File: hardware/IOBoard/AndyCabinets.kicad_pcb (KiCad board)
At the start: 2 copper layers, 44.5 x 76.2 mm, 47 parts, among them SW1 Mode_Encoder, SW2 Color_Encoder, U1 74HC14

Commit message: After PCB v2
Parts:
- removed C9: 1uF, Capacitor_SMD:C_0805_2012Metric
- C11, C13: value 0.01uF -> 0.1uF
- moved C6 47.8 mm to (176.1, 115.9)
- moved R2 47.8 mm to (176.1, 120.0)
- moved R6 47.8 mm to (176.1, 117.9)
- moved C5 47.7 mm to (177.8, 115.9)
- moved R1 47.7 mm to (177.8, 120.0)
- moved R5 47.7 mm to (177.8, 117.9)
- moved C11 47.3 mm to (179.5, 115.9)
- moved R10 47.3 mm to (179.5, 117.9)
- moved R9 47.3 mm to (179.5, 120.0)
- moved C7 30.3 mm to (216.1, 64.9), turned to 0 degrees
- moved C8 29.0 mm to (216.1, 66.4), turned to 0 degrees
- moved R7 28.6 mm to (214.1, 64.9), turned to 0 degrees
- moved C13 27.7 mm to (216.1, 67.8), turned to 0 degrees
- moved R8 27.2 mm to (214.1, 66.4), turned to 180 degrees
- moved R3 27.2 mm to (212.0, 64.9), turned to 0 degrees
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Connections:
- U1 pad 12: Net-(C13-Pad1) -> /GPIO32_MODE_BTN
- U1 pad 13: /GPIO32_MODE_BTN -> Net-(C13-Pad1)
- U1 pad 3: /GPIO33_MODE_B -> Net-(C7-Pad1)
- U1 pad 4: Net-(C7-Pad1) -> /GPIO33_MODE_B
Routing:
- net +3V3: track 122.2 -> 48.3 mm, vias 13 -> 1
- net Net-(C5-Pad1): track 38.5 -> 84.1 mm, vias 0 -> 2
- net Net-(C11-Pad1): track 32.2 -> 77.5 mm, vias 0 -> 2
- net Net-(C6-Pad1): track 36.3 -> 81.0 mm, vias 0 -> 4
- net Net-(R10-Pad2): track 60.7 -> 17.5 mm, vias 0 -> 1
- net Net-(R1-Pad2): track 54.0 -> 18.8 mm, vias 0 -> 2
- net Net-(R2-Pad2): track 48.8 -> 17.5 mm, vias 0 -> 2
- net Net-(C8-Pad1): track 40.5 -> 14.6 mm, vias 0 -> 2
- net GNDD: track 74.3 -> 99.1 mm, vias 21 -> 20
- net Net-(C13-Pad1): track 34.2 -> 9.48 mm, vias 0 -> 2
- net +5V: track 46.3 -> 22.6 mm
- net /GPIO35_COLOR_BTN: track 50.9 -> 27.8 mm
- net /GPIO32_MODE_BTN: track 33.1 -> 12.3 mm
- net /GPIO39_COLOR_A: track 44.9 -> 26.5 mm
- net Net-(R3-Pad2): track 24.3 -> 42.1 mm, vias 0 -> 3
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- added copper zone on F.Cu, net +3V3
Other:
- board size 44.5 x 76.2 mm -> 44.4 x 70 mm
- net class Default: clearance 0.1016 -> 0.1524; trace_width 0.127 -> 0.2032
- net class Power: clearance 0.2 -> 0.1524; trace_width 0.5 -> 0.3556
- rule trace_clearance: 0.1016 -> 0.1524

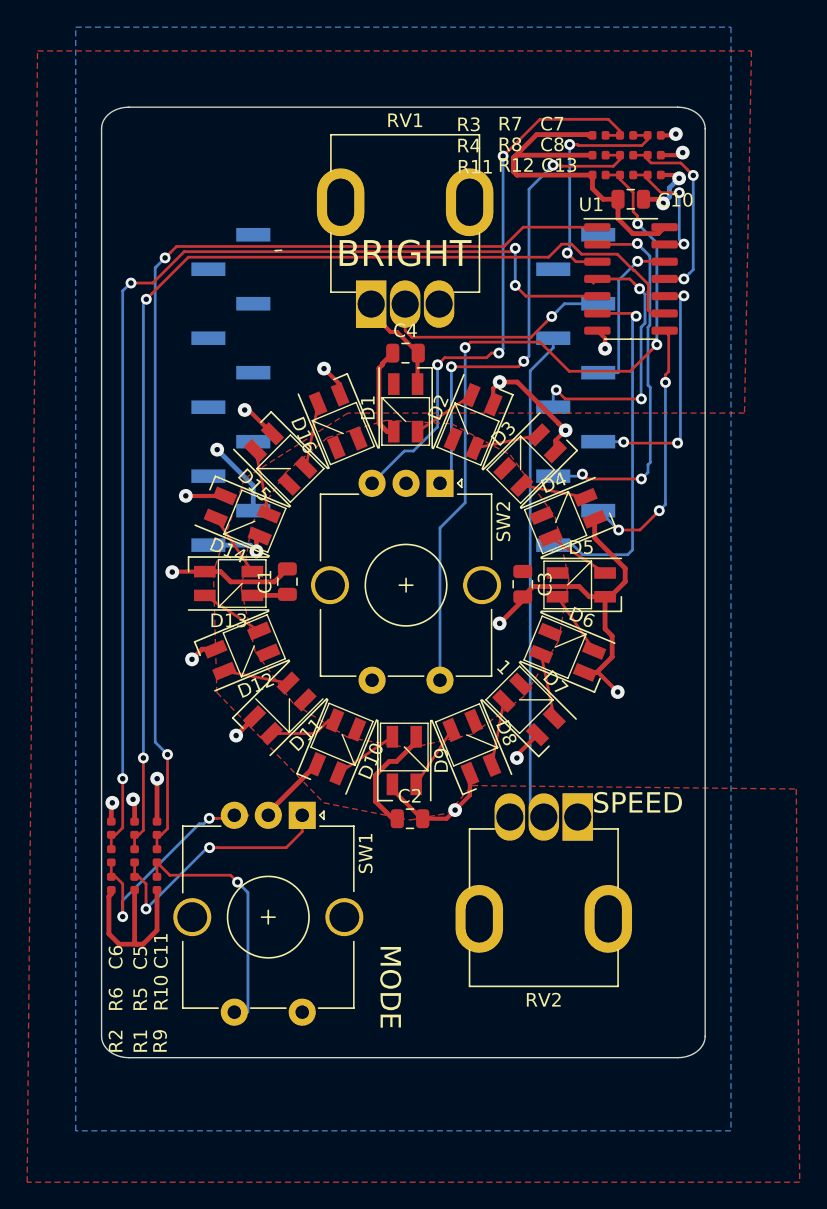
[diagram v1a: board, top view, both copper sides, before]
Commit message: Initial working remote version; some minor PCB changes
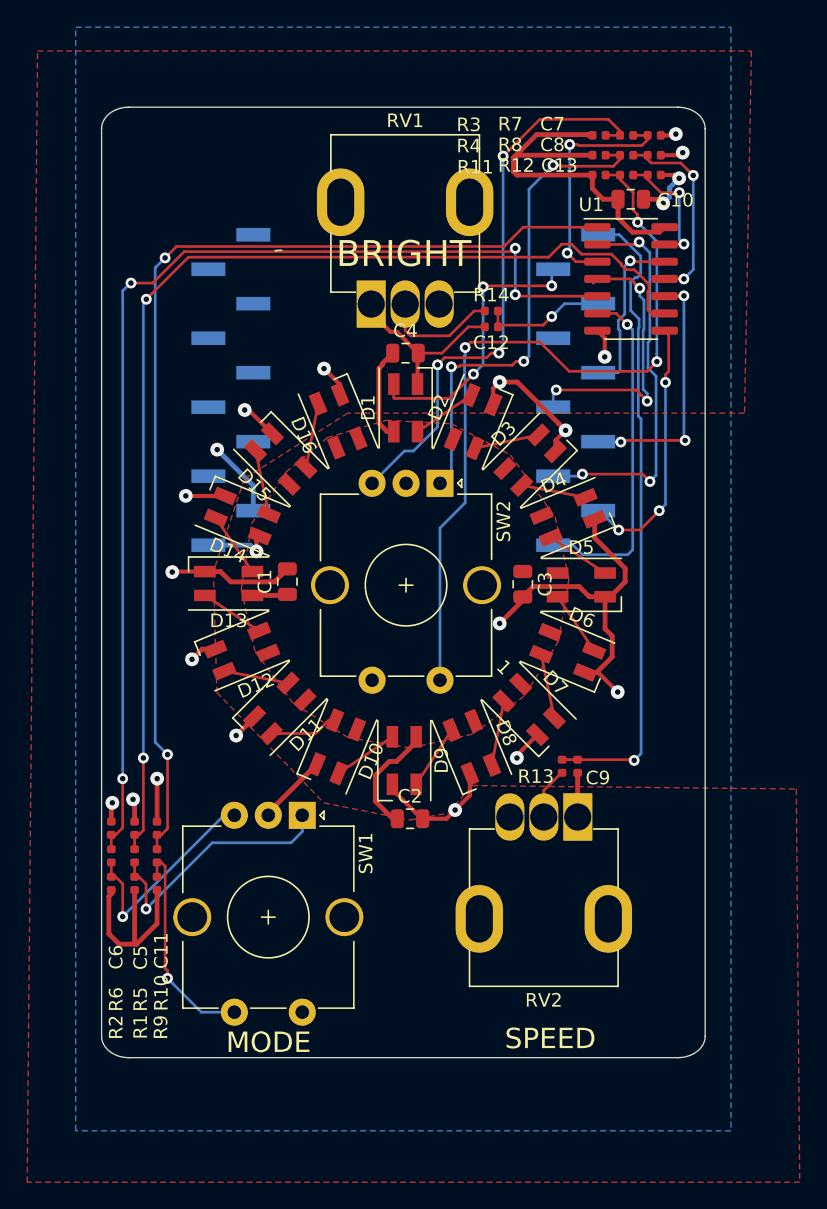
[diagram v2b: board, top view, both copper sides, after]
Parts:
- added C12: 0.1uF, Capacitor_SMD:C_0402_1005Metric, F.Cu at (204.1, 79.0)
- added C9: 0.1uF, Capacitor_SMD:C_0402_1005Metric, F.Cu at (210.5, 111.4)
- added R13: 10K, Resistor_SMD:R_0402_1005Metric, F.Cu at (209.3, 111.4)
- added R14: 10K, Resistor_SMD:R_0402_1005Metric, F.Cu at (204.1, 77.8)
- C5, C6: value 0.01uF -> 0.1uF
- RV1: value Speed_Pot -> BrightPot
- RV2: value Bright_Pot -> SpeedPot
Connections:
- net /GPIO32_MODE_BTN renamed /GPIO32_COLOR_BTN
- net /GPIO33_MODE_B renamed /GPIO33_COLOR_B
- net /GPIO34_MODE_A renamed /GPIO34_COLOR_A
- net /GPIO35_COLOR_BTN renamed /GPIO35_MODE_BTN
- net /GPIO36_COLOR_B renamed /GPIO36_MODE_A
- net /GPIO39_COLOR_A renamed /GPIO39_MODE_B
- D1 pad 4: /GPIO32_PREVIEW -> /GPIO14_PREVIEW
- EXT2 pad 10: /GPIO13/I2C-SDA -> /GPIO13_SPEED
- EXT2 pad 7: /GPIO16_BRIGHT -> /GPIO16
- EXT2 pad 8: /GPIO15_SPEED -> /GPIO15_BRIGHT
- EXT2 pad 9: /GPIO14/HS2_CLK -> /GPIO14_PREVIEW
- RV1 pad 2: /GPIO15_SPEED -> Net-(R14-Pad1)
- RV2 pad 2: /GPIO16_BRIGHT -> Net-(R13-Pad1)
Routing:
- net /GPIO13_SPEED: track 0.00 -> 47.2 mm, vias 0 -> 1
- net /GPIO16_BRIGHT: track 36.0 -> 0.00 mm
- net /GPIO14_PREVIEW: track 0.00 -> 20.7 mm, vias 0 -> 3
- net /GPIO15_SPEED: track 17.4 -> 0.00 mm, vias 1 -> 0
- net /GPIO15_BRIGHT: track 0.00 -> 9.60 mm, vias 0 -> 1
- net GNDD: track 99.1 -> 108.6 mm
- net Net-(R14-Pad1): track 0.00 -> 8.73 mm
- net Net-(R13-Pad1): track 0.00 -> 3.84 mm
- net Net-(R2-Pad2): track 17.5 -> 15.8 mm, vias 2 -> 1
- net Net-(R10-Pad2): track 17.5 -> 16.1 mm
- net /GPIO35_MODE_BTN: track 27.8 -> 29.0 mm
- net /GPIO39_MODE_B: track 26.5 -> 25.6 mm
- net Net-(R11-Pad2): track 55.9 -> 56.7 mm
- net /GPIO33_COLOR_B: track 21.1 -> 21.9 mm
- net Net-(R1-Pad2): track 18.8 -> 19.0 mm, vias 2 -> 1
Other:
- board text added: "13 BRIGHT"
- board text added: "14 PREVIEW"
- board text removed: "HS2_CLK"
- board text removed: "I2C-SDA"

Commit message: Rev 3 PCB
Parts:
- added J1: wESP Connector, YonaFootprints:PinSocket_2x10_P2.54mm_Vertical_SMD_Mirror, B.Cu at (197.6, 129.7)
- added JP1: wESP Power Jumper, Jumper:SolderJumper-2_P1.3mm_Open_TrianglePad1.0x1.5mm, B.Cu at (198.1, 122.4)
- SW1: value Mode_Encoder -> Color_Encoder; footprint Rotary_Encoder:RotaryEncoder_Alps_EC12E-Switch_Vertical_H20mm_CircularMountingHoles -> YonaFootprints:RotaryEncoder_Alps_EC12E-SMDSwitch_Vertical_H20mm_CircularMountingHoles
- SW2: value Color_Encoder -> Mode_Encoder
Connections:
- net /GPIO14_PREVIEW renamed /GPIO14
- net /GPIO32_COLOR_BTN renamed /GPIO32
- net /GPIO35_MODE_BTN renamed /COLOR_BTN
- net /GPIO36_MODE_A renamed /COLOR_A
- net /GPIO39_MODE_B renamed /COLOR_B
- C12 pad 1: /GPIO15_BRIGHT -> /BRIGHT
- C9 pad 1: /GPIO13_SPEED -> /GPIO33
- EXT2 pad 10: /GPIO13_SPEED -> /GPIO13
- EXT2 pad 4: /GPIO34_COLOR_A -> /BRIGHT
- EXT2 pad 5: /GPIO33_COLOR_B -> /GPIO33
- EXT2 pad 8: /GPIO15_BRIGHT -> /GPIO15
- R13 pad 2: /GPIO13_SPEED -> /GPIO33
- R14 pad 2: /GPIO15_BRIGHT -> /BRIGHT
- U1 pad 10: /GPIO34_COLOR_A -> /GPIO15
- U1 pad 4: /GPIO33_COLOR_B -> /GPIO13
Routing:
- net /GPIO13: track 0.00 -> 95.3 mm, vias 0 -> 5
- net /GPIO15: track 0.00 -> 94.3 mm, vias 0 -> 4
- net /GPIO14: track 20.7 -> 102.9 mm, vias 3 -> 6
- net /GPIO33: track 0.00 -> 74.3 mm, vias 0 -> 5
- net /BRIGHT: track 0.00 -> 66.9 mm, vias 0 -> 5
- net /GPIO32: track 12.7 -> 77.3 mm, vias 1 -> 5
- net /COLOR_BTN: track 29.0 -> 85.7 mm, vias 3 -> 5
- net /COLOR_B: track 25.6 -> 75.5 mm, vias 1 -> 5
- net /GPIO13_SPEED: track 47.2 -> 0.00 mm, vias 1 -> 0
- net /COLOR_A: track 19.3 -> 61.1 mm, vias 3 -> 5
- net /GPIO33_COLOR_B: track 21.9 -> 0.00 mm, vias 3 -> 0
- net /GPIO34_COLOR_A: track 18.6 -> 0.00 mm, vias 3 -> 0
- net +5V: track 22.6 -> 39.5 mm, vias 1 -> 2
- net /wESP_V+: track 0.00 -> 13.9 mm
- net /GPIO15_BRIGHT: track 9.60 -> 0.00 mm, vias 1 -> 0
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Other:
- board size 44.4 x 70 mm -> 44.4 x 71.4 mm
- board text added: "13 MODE_B"
- board text added: "15 MODE_A"
- board text added: "16 N/C"
- board text added: "32 MODE_BTN"
- board text added: "33 SPEED"
- board text added: "34 BRIGHT"
- board text added: "35 COLOR_BTN"
- board text added: "36 COLOR_A"
- board text added: "39 COLOR_B"
- board text added: "COLOR"
- board text added: "V+"
- board text added: "wESP"
- board text removed: "13 BRIGHT"
- board text removed: "15 SPEED"
- board text removed: "16 BRIGHT"
- board text removed: "30 COLOR B"
- board text removed: "32"
- board text removed: "33 MODE B"
- board text removed: "34 MODE A"
- board text removed: "35 COLOR"
- board text removed: "39 COLOR A"

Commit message: Hardware pre change to SMD2020
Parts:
- SW2: footprint Rotary_Encoder:RotaryEncoder_Alps_EC12E-Switch_Vertical_H20mm_CircularMountingHoles -> YonaFootprints:RotaryEncoder_Alps_EC12E-Switch_Vertical_H20mm_CircularMountingHoles_ReducedFootprint
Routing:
- net +5V: track 39.5 -> 40.4 mm
